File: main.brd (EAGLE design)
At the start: 100 x 80 mm, 26 parts, among them IC1 7805TV, IC2 L293D, U1 ATMEGA328P_TQFP

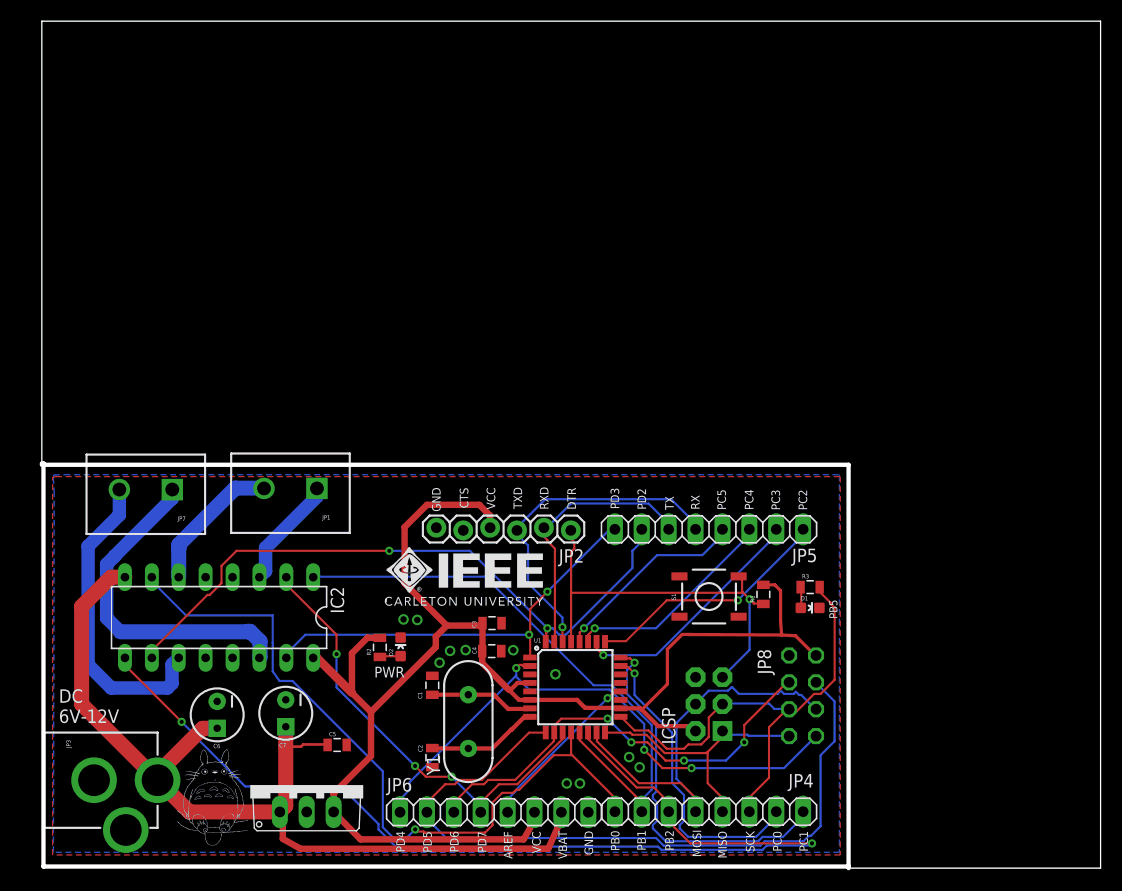
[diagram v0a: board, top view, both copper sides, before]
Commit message: Work in progress commit for r1.1
1. Changed VREG to smaller package
2. Added RST decoupling capacitor
3. Added idiot diode
4. Removed motor controller and support circuitry.
5. Added additional decoupling capacitor
6. Reworked board outline
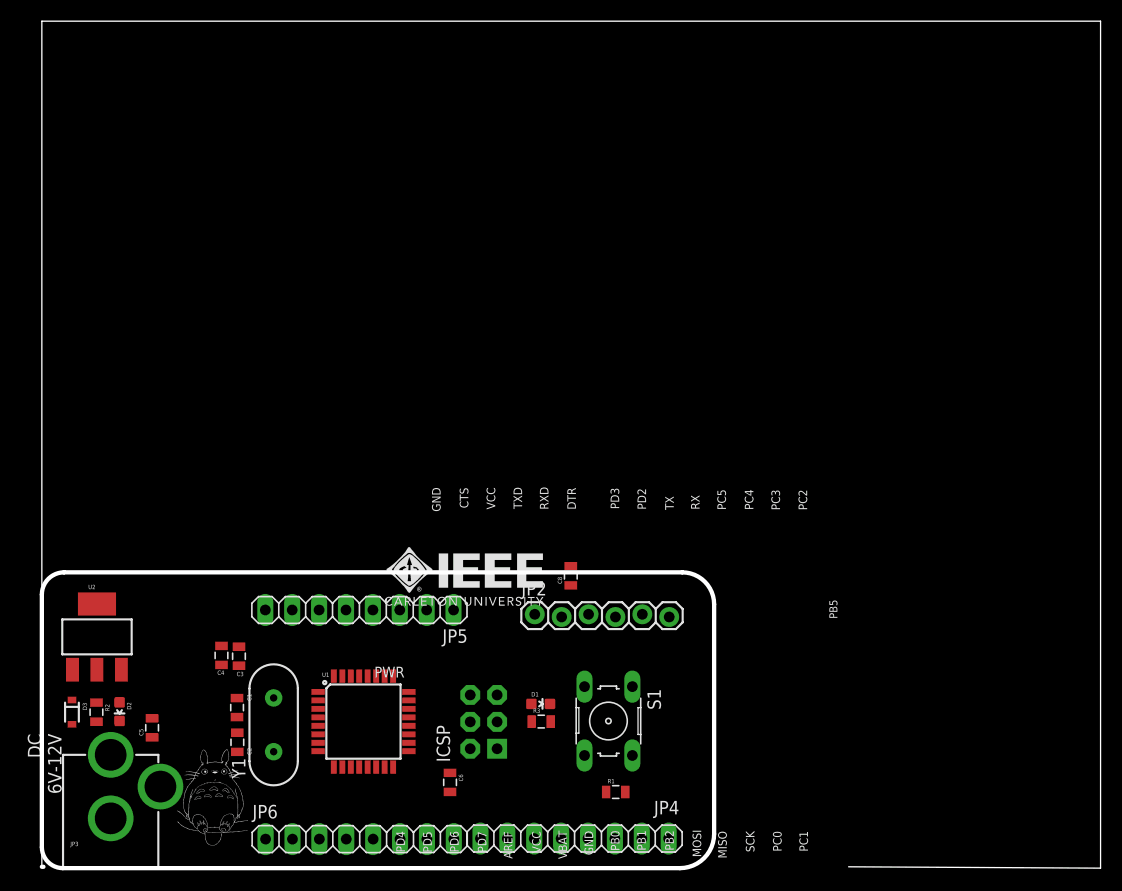
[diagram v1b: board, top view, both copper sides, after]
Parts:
- removed C7: (no value), SparkFun-Passives:CPOL-RADIAL-10UF-25V
- removed IC1: 7805TV, linear:TO220V
- removed IC2: L293D, st-microelectronics:DIL16
- removed JP1, JP7: (no value), SparkFun-Connectors:SCREWTERMINAL-5MM-2
- removed JP8: (no value), pinhead:2X04
- added C8: (no value), SparkFun-Passives:0805
- added D3: 250mA/100V, SparkFun-DiscreteSemi:SOD-323
- added U2: (no value), SparkFun-PowerIC:SOT223
- C6: device SparkFun-Passives:CPOL-RADIAL-10UF-25V -> SparkFun-Passives:0805
- S1: value SWITCH-MOMENTARY-2SMD -> (none); device SparkFun-Electromechanical:TACTILE-SWITCH-SMD -> switch-omron:B3F-10XX
- moved JP5 33.9 mm to (30.0, 24.4)
- moved R3 28.4 mm to (47.2, 13.8)
- moved R2 27.5 mm to (5.16, 14.7), turned to 270 degrees
- moved D2 27.2 mm to (7.34, 14.8), turned to 180 degrees
- moved D1 27.0 mm to (47.1, 15.5)
- moved C4 25.5 mm to (17.0, 20.1), turned to 90 degrees
- moved C3 24.1 mm to (18.6, 20.0), turned to 90 degrees
- moved R1 23.3 mm to (54.2, 7.19), turned to 0 degrees
- moved C6 22.9 mm to (38.6, 8.10)
- moved ICSP 21.4 mm to (41.7, 13.8)
- moved U1 20.3 mm to (30.4, 13.8)
- moved C1 18.6 mm to (18.4, 15.2), turned to 270 degrees
- moved C2 18.5 mm to (18.5, 11.9), turned to 90 degrees
- moved Y1 18.4 mm to (21.9, 13.5)
- moved C5 17.6 mm to (10.4, 13.3), turned to 90 degrees
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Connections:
- net N$1 renamed XTAL_P
- net N$2 renamed XTAL_N
- removed net MOT1+: IC2.3, JP1.1
- removed net MOT1-: IC2.6, JP1.2
- removed net MOT2+: IC2.14, JP7.1
- removed net MOT2-: IC2.11, JP7.2
- new net N$5: C8.2, JP2.1
- net GND: now also D3.A, S1.3, S1.4, U2.1; no longer C7.2, IC1.2, IC2.12, IC2.13, IC2.4, IC2.5, JP8.2, S1.1
- net MISO: no longer JP8.8
- net MOSI: no longer JP8.5
- net PB0: no longer IC2.7
- net PB1: no longer IC2.1
- net PB2: no longer IC2.9
- net PD2: no longer IC2.10
- net PD3: no longer IC2.15
- net PD4: no longer JP8.7
- net PD5: no longer JP8.3
- net PD6: no longer JP8.4
- net PD7: no longer IC2.2
- net RST: now also C8.1, S1.1, S1.2; no longer JP2.1, S1.3
- net SCK: no longer JP8.6
- net VBAT: now also U2.3; no longer C6.1, C7.1, IC1.1, IC2.8
- net VCC: now also C6.1, D3.C, U2.2, U2.4; no longer IC1.3, IC2.16, JP8.1
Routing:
- net VCC: track 140.4 -> 0.00 mm
- net PB2: track 100.3 -> 0.00 mm, vias 2 -> 0
- net VBAT: track 90.2 -> 0.00 mm
- net PB0: track 70.3 -> 0.00 mm, vias 1 -> 0
- net PD5: track 69.3 -> 0.00 mm
- net PD2: track 62.2 -> 0.00 mm, vias 2 -> 0
- net PB1: track 56.3 -> 0.00 mm
- net PD4: track 54.3 -> 0.00 mm, vias 3 -> 0
- net SCK: track 46.5 -> 0.00 mm
- net PD7: track 43.0 -> 0.00 mm, vias 3 -> 0
- net PD6: track 42.4 -> 0.00 mm, vias 4 -> 0
- net PD3: track 39.9 -> 0.00 mm, vias 2 -> 0
- net RST: track 39.5 -> 0.00 mm, vias 1 -> 0
- net MOSI: track 38.7 -> 0.00 mm
- net PC1: track 35.2 -> 0.00 mm, vias 1 -> 0
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- removed copper zone on layer 1, net GND
- removed copper zone on layer 16, net GND
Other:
- outline, holes or cut-outs redrawn

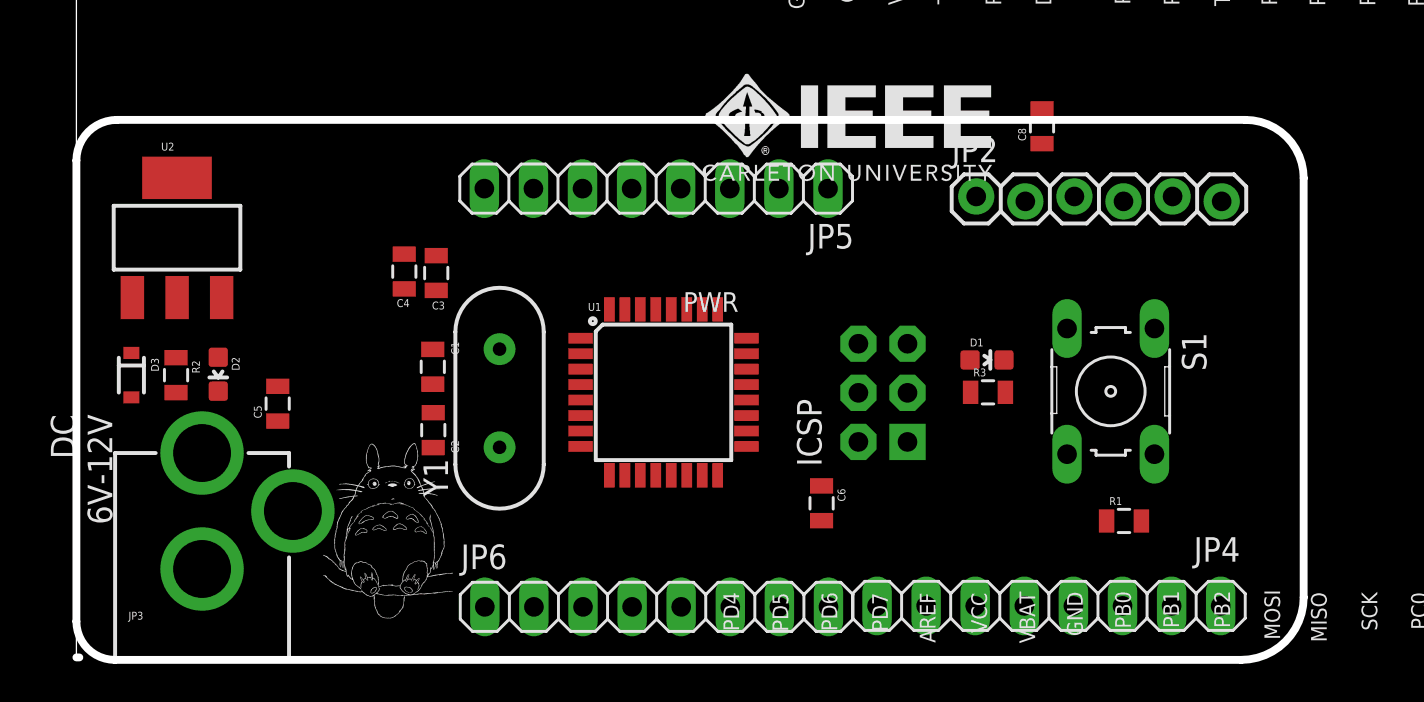
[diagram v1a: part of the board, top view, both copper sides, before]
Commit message: Added UART-USB Chip
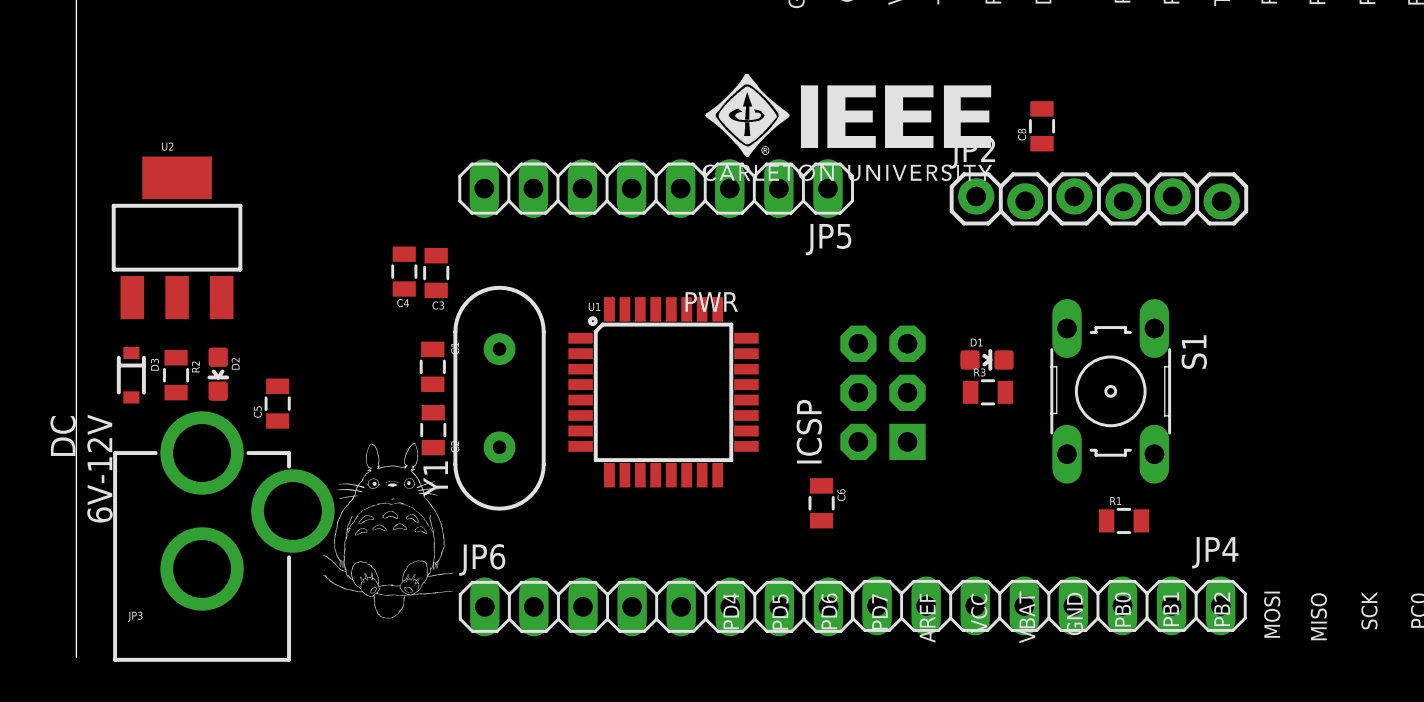
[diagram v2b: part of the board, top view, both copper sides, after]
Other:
- outline, holes or cut-outs redrawn
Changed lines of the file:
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@@
 <?xml version="1.0" encoding="utf-8"?>
 <!DOCTYPE eagle SYSTEM "eagle.dtd">
-<eagle version="7.3.0">
+<eagle version="8.0.1">
 <drawing>
 <settings>
@@
 <wire x1="100" y1="80" x2="0" y2="80" width="0" layer="20"/>
 <wire x1="0" y1="80" x2="0" y2="0.127" width="0" layer="20"/>
-<wire x1="0" y1="0.127" x2="0.1524" y2="0.127" width="0.4064" layer="20"/>
 <text x="36.8554" y="35.9664" size="0.8128" layer="21" rot="R270">GND</text>
 <text x="39.4716" y="35.941" size="0.8128" layer="21" rot="R270">CTS</text>
@@
 <text x="-1.3208" y="12.7" size="1.27" layer="21" font="vector" ratio="15" rot="R270">DC
 6V-12V</text>
-<wire x1="60.26910625" y1="0" x2="1.99110625" y2="0" width="0.4064" layer="20"/>
-<wire x1="1.99110625" y1="0" x2="0" y2="1.99110625" width="0.4064" layer="20" curve="-90"/>
-<wire x1="0" y1="1.99110625" x2="0" y2="25.8403875" width="0.4064" layer="20"/>
-<wire x1="0" y1="25.8403875" x2="2.0996125" y2="27.94" width="0.4064" layer="20" curve="-90"/>
-<wire x1="2.0996125" y1="27.94" x2="60.488521875" y2="27.94" width="0.4064" layer="20"/>
-<wire x1="60.488521875" y1="27.94" x2="63.5" y2="24.928521875" width="0.4064" layer="20" curve="-90"/>
-<wire x1="63.5" y1="24.928521875" x2="63.5" y2="3.23089375" width="0.4064" layer="20"/>
-<wire x1="63.5" y1="3.23089375" x2="60.26910625" y2="0" width="0.4064" layer="20" curve="-90"/>
 </plain>
 <attributes>

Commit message: Board layout made
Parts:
- removed C1, C3, C8: (no value), SparkFun-Passives:0805
- removed D2: BLUE, SparkFun-LED:LED-0603
- removed JP3: POWER_JACKPTH, SparkFun-Connectors:POWER_JACK_PTH
- removed R1: (no value), SparkFun-Resistors:0805
- removed U2: (no value), SparkFun-PowerIC:SOT223
- removed Y1: (no value), SparkFun-FreqCtrl:HC49US
- added C11: 4.7uF, SparkFun-Capacitors:0603-POLAR
- added C7: 0.1uF, SparkFun-Capacitors:0603
- added D4: RED, SparkFun-LED:LED-0603
- added D7: GREEN, SparkFun-LED:LED-0603
- added F1: 6V/0.5A, SparkFun-Fuses:1206
- added IC1: FT232RL, ftdichip:SSOP28
- added J1: (no value), SparkFun-Connectors:USB-B-MICRO-SMD
- added R4, R5, R7, R8: 1k, SparkFun-Resistors:0805
- added Y3: 16MHz, SparkFun-Clocks:HC49US
- C2, C6: value (none) -> 0.1uF; device SparkFun-Passives:0805 -> SparkFun-Capacitors:0603
- C4, C5: value (none) -> 22pF; device SparkFun-Passives:0805 -> SparkFun-Capacitors:0603
- D3: value 250mA/100V -> 2A/100V/850mV; device SparkFun-DiscreteSemi:SOD-323 -> SparkFun-DiscreteSemi:SMA-DIODE
- R2, R3: value (none) -> 1k
- U1: device SparkFun-DigitalIC:TQFP32-08 -> SparkFun-IC-Microcontroller:TQFP32-08
- moved JP4 50.3 mm to (10.2, 33.0), turned to 180 degrees
- moved S1 45.5 mm to (8.89, 5.08), turned to 0 degrees
- moved R3 40.1 mm to (7.62, 20.3), flipped to the bottom, turned to 90 degrees
- moved JP6 31.3 mm to (38.1, 33.0), turned to 180 degrees
- moved D1 29.5 mm to (17.8, 19.1), turned to 180 degrees
- moved C6 27.9 mm to (17.8, 26.7), turned to 90 degrees
- moved D3 26.6 mm to (26.7, 26.7)
- moved C5 24.9 mm to (34.3, 20.3), turned to 270 degrees
- moved JP5 22.1 mm to (26.7, 2.54), turned to 0 degrees
- moved JP2 21.4 mm to (47.0, 2.54), turned to 90 degrees
- moved C4 18.4 mm to (34.3, 14.0)
- moved ICSP 13.1 mm to (44.5, 26.7), turned to 0 degrees
- moved C2 10.9 mm to (7.62, 12.7), flipped to the bottom
- moved U1 4.57 mm to (26.7, 16.5), turned to 180 degrees
- moved R2 3.04 mm to (7.62, 16.5), flipped to the bottom
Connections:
- removed net N$4: D1.A, R3.1
- removed net N$5: C8.2, JP2.1
- new net 3.3V: C6.2, IC1.17
- new net 5V: D1.A, D3.C, D4.A, R2.2, R3.2, R7.2, R8.2
- new net CBUS0: IC1.23, R2.1
- new net CBUS1: IC1.22, R3.1
- new net N$15: IC1.20, IC1.4
- new net N$17: U1.21, U1.3, U1.5
- new net N$19: J1.GND
- new net N$20: J1.SHIELD1, J1.SHIELD2, J1.SHIELD3
- new net N$21: IC1.18, IC1.21, IC1.26, IC1.7
- new net N$22: IC1.25
- new net N$7: C2.2, IC1.19
- new net USBD+: IC1.15, J1.D+
- new net USBD-: IC1.16, J1.D-
- new net VBUS: F1.2, J1.VBUS
- new net V_USB: C11.+, C7.2, D3.A, F1.1
- net GND: now also C11.-, C4.1, C5.1, C6.1, C7.1, D7.C; no longer C1.2, C2.2, C3.2, C4.2, C5.2, C6.2, D1.C, D2.C, D3.A, JP3.GND, JP3.GNDBREAK, U1.21, U1.3, U1.5, U2.1
- net N$3: now also D7.A, R7.1; no longer D2.A, R2.1
- net RST: now also C2.1, JP2.1, R8.1; no longer C8.1, R1.1
- net RX: now also D1.C, IC1.1, R4.1, R4.2
- net SCK: no longer R3.2
- net TX: now also D4.C, IC1.5, R5.1, R5.2
- net VBAT: no longer C5.1, JP3.PWR, U2.3
- net VCC: no longer C3.1, C4.1, C6.1, D3.C, R1.2, R2.2, U2.2, U2.4
- net XTAL_N: now also C5.2, Y3.2; no longer C2.1, Y1.1
- net XTAL_P: now also C4.2, Y3.1; no longer C1.1, Y1.2
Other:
- board size 100 x 80 mm -> 49.5 x 35.6 mm
- board text removed: "AREF"
- board text removed: "CTS"
- board text removed: "DC 6V-12V"
- board text removed: "DTR"
- board text removed: "GND"
- board text removed: "Hasith Vidanamadura hasith@vidanamadura.net, 2015"
- board text removed: "MISO"
- board text removed: "MOSI"
- board text removed: "PB0"
- board text removed: "PB1"
- board text removed: "PB2"
- board text removed: "PB5"
- board text removed: "PC0"
- board text removed: "PC1"
- board text removed: "PC2"
- board text removed: "PC3"
- board text removed: "PC4"
- board text removed: "PC5"
- board text removed: "PD2"
- board text removed: "PD3"
- board text removed: "PD4"
- board text removed: "PD5"
- board text removed: "PD6"
- board text removed: "PD7"
- board text removed: "PWR"
- board text removed: "RX"
- board text removed: "RXD"
- board text removed: "SCK"
- board text removed: "TX"
- board text removed: "TXD"
- board text removed: "VBAT"
- board text removed: "VCC"

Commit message: Diff lines routed
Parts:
- moved JP2 1.27 mm to (47.0, 3.81)
- moved JP5 1.27 mm to (26.7, 3.81)
- moved C5 1.27 mm to (34.3, 19.1)
- moved JP4 1.27 mm to (11.4, 33.0)
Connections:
- net USBD+ renamed USBD_P
- net USBD- renamed USBD_N
- removed net N$15: IC1.20, IC1.4
- removed net N$17: U1.21, U1.3, U1.5
- removed net N$19: J1.GND
- removed net N$20: J1.SHIELD1, J1.SHIELD2, J1.SHIELD3
- removed net N$21: IC1.18, IC1.21, IC1.26, IC1.7
- removed net N$22: IC1.25
- removed net VBAT: JP6.7
- net 5V: now also IC1.20, IC1.4
- net GND: now also IC1.18, IC1.21, IC1.25, IC1.26, IC1.7, J1.GND, J1.SHIELD1, J1.SHIELD2, J1.SHIELD3, U1.21, U1.3, U1.5
- net RX: now also IC1.5, R5.2
- net TX: no longer IC1.5, R5.2
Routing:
- net XTAL_P: track 0.00 -> 12.5 mm
- net XTAL_N: track 0.00 -> 12.3 mm
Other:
- board size 49.5 x 35.6 mm -> 49.5 x 36.8 mm
